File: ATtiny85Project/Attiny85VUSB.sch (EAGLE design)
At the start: 26 parts

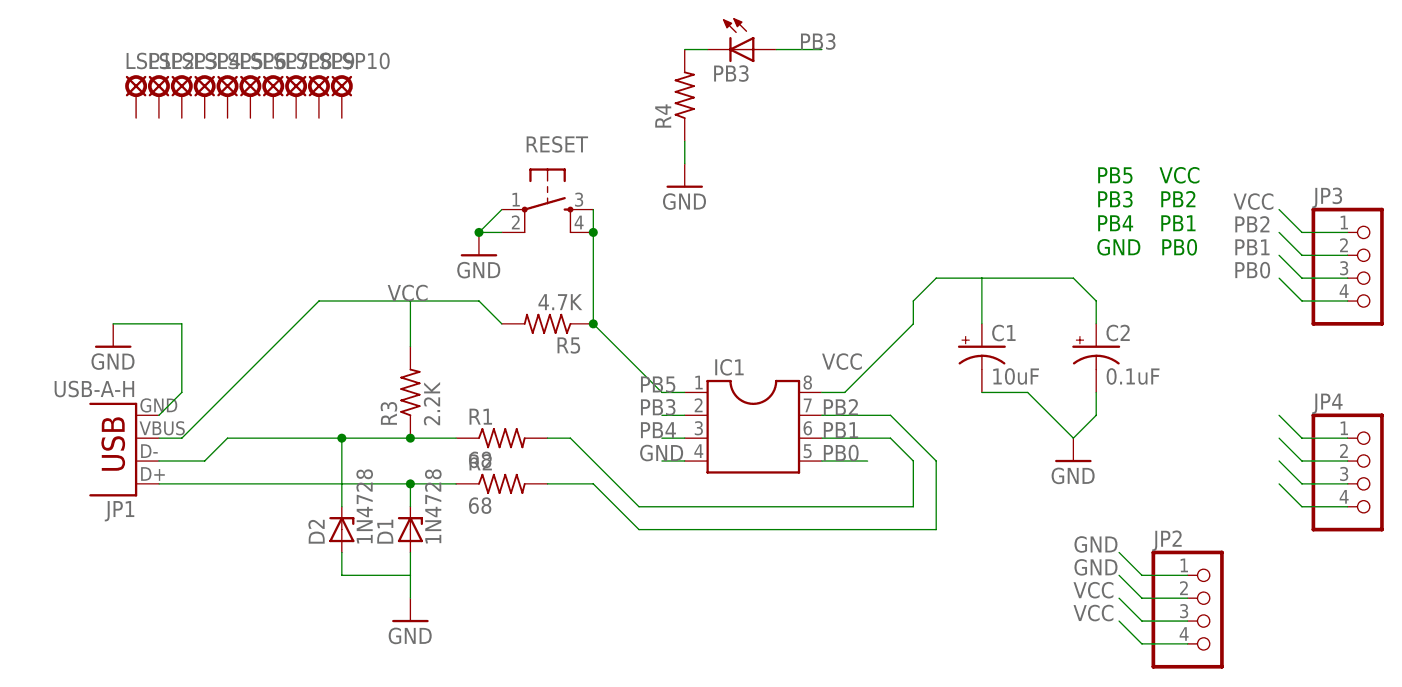
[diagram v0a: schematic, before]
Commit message: Small fixes to attiny85 to use other pins
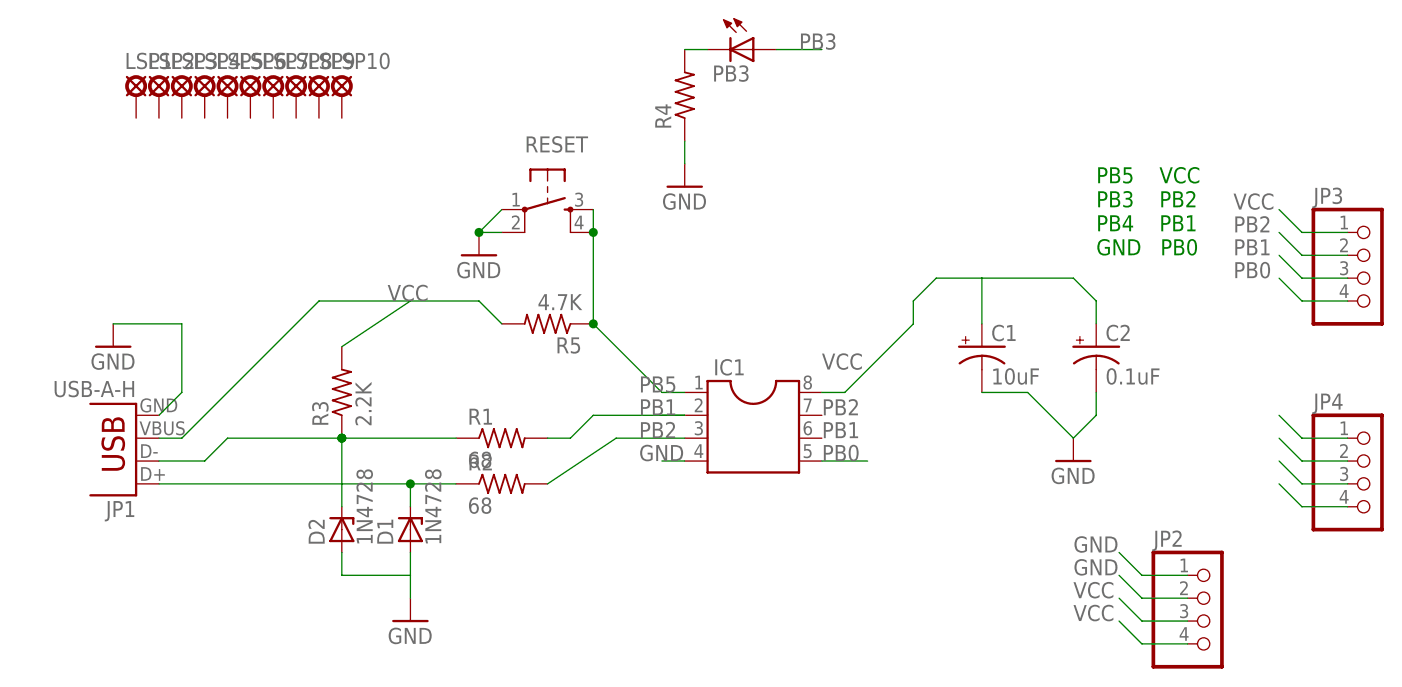
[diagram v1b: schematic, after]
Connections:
- net N$1 renamed DMIN
- net N$4 renamed DPLUS
- net PB1: now also IC1.PB3_CLKI; no longer IC1.PB1_MISO
- net PB2: now also IC1.PB4_CLKO; no longer IC1.PB2SCK
- net PB3: no longer IC1.PB3_CLKI
- net PB4: no longer IC1.PB4_CLKO
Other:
- moved on the sheet: R3
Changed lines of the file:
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@@
 <?xml version="1.0" encoding="utf-8"?>
 <!DOCTYPE eagle SYSTEM "eagle.dtd">
-<eagle version="6.5.0">
+<eagle version="7.5.0">
 <drawing>
 <settings>
@@
 <instance part="R1" gate="G$1" x="7.62" y="68.58"/>
 <instance part="R2" gate="G$1" x="7.62" y="63.5"/>
-<instance part="R3" gate="G$1" x="-2.54" y="73.66" rot="R90"/>
+<instance part="R3" gate="G$1" x="-10.16" y="73.66" rot="R90"/>
 <instance part="D1" gate="1" x="-2.54" y="58.42" rot="R90"/>
 <instance part="D2" gate="1" x="-10.16" y="58.42" rot="R90"/>
@@
 <net name="PB1" class="0">
 <segment>
-<pinref part="IC1" gate="G$1" pin="PB1_MISO"/>
-<wire x1="43.18" y1="68.58" x2="50.8" y2="68.58" width="0.1524" layer="91"/>
-<wire x1="50.8" y1="68.58" x2="53.34" y2="66.04" width="0.1524" layer="91"/>
-<wire x1="53.34" y1="66.04" x2="53.34" y2="60.96" width="0.1524" layer="91"/>
-<wire x1="53.34" y1="60.96" x2="22.86" y2="60.96" width="0.1524" layer="91"/>
-<wire x1="22.86" y1="60.96" x2="15.24" y2="68.58" width="0.1524" layer="91"/>
 <pinref part="R1" gate="G$1" pin="2"/>
-<wire x1="15.24" y1="68.58" x2="12.7" y2="68.58" width="0.1524" layer="91"/>
 <label x="43.18" y="68.58" size="1.778" layer="95"/>
+<wire x1="12.7" y1="68.58" x2="15.24" y2="68.58" width="0.1524" layer="91"/>
+<wire x1="15.24" y1="68.58" x2="17.78" y2="71.12" width="0.1524" layer="91"/>
+<pinref part="IC1" gate="G$1" pin="PB3_CLKI"/>
+<wire x1="27.94" y1="71.12" x2="25.4" y2="71.12" width="0.1524" layer="91"/>
+<label x="22.86" y="71.12" size="1.778" layer="95"/>
+<wire x1="17.78" y1="71.12" x2="27.94" y2="71.12" width="0.1524" layer="91"/>
 </segment>
 <segment>
@@
 <net name="PB2" class="0">
 <segment>
-<pinref part="IC1" gate="G$1" pin="PB2SCK"/>
-<wire x1="43.18" y1="71.12" x2="50.8" y2="71.12" width="0.1524" layer="91"/>
-<wire x1="50.8" y1="71.12" x2="55.88" y2="66.04" width="0.1524" layer="91"/>
-<wire x1="55.88" y1="66.04" x2="55.88" y2="58.42" width="0.1524" layer="91"/>
-<wire x1="55.88" y1="58.42" x2="22.86" y2="58.42" width="0.1524" layer="91"/>
-<wire x1="22.86" y1="58.42" x2="17.78" y2="63.5" width="0.1524" layer="91"/>
 <pinref part="R2" gate="G$1" pin="2"/>
-<wire x1="17.78" y1="63.5" x2="12.7" y2="63.5" width="0.1524" layer="91"/>
 <label x="43.18" y="71.12" size="1.778" layer="95"/>
+<pinref part="IC1" gate="G$1" pin="PB4_CLKO"/>
+<wire x1="27.94" y1="68.58" x2="20.32" y2="68.58" width="0.1524" layer="91"/>
+<label x="22.86" y="68.58" size="1.778" layer="95"/>
+<wire x1="12.7" y1="63.5" x2="20.32" y2="68.58" width="0.1524" layer="91"/>
 </segment>
 <segment>
@@
 </segment>
 </net>
-<net name="N$4" class="0">
+<net name="DPLUS" class="0">
 <segment>
 <pinref part="R2" gate="G$1" pin="1"/>
@@
 </segment>
 </net>
-<net name="N$1" class="0">
+<net name="DMIN" class="0">
 <segment>
 <pinref part="R1" gate="G$1" pin="1"/>
 <pinref part="R3" gate="G$1" pin="1"/>
-<wire x1="2.54" y1="68.58" x2="-2.54" y2="68.58" width="0.1524" layer="91"/>
+<wire x1="2.54" y1="68.58" x2="-10.16" y2="68.58" width="0.1524" layer="91"/>
 <pinref part="D2" gate="1" pin="C"/>
-<wire x1="-2.54" y1="68.58" x2="-10.16" y2="68.58" width="0.1524" layer="91"/>
 <wire x1="-10.16" y1="68.58" x2="-10.16" y2="60.96" width="0.1524" layer="91"/>
 <wire x1="-10.16" y1="68.58" x2="-22.86" y2="68.58" width="0.1524" layer="91"/>
@@
 <wire x1="-25.4" y1="66.04" x2="-30.48" y2="66.04" width="0.1524" layer="91"/>
 <junction x="-10.16" y="68.58"/>
-<junction x="-2.54" y="68.58"/>
+<junction x="-10.16" y="68.58"/>
 </segment>
 </net>
@@
 <segment>
 <pinref part="R3" gate="G$1" pin="2"/>
-<wire x1="-2.54" y1="78.74" x2="-2.54" y2="83.82" width="0.1524" layer="91"/>
+<wire x1="-10.16" y1="78.74" x2="-2.54" y2="83.82" width="0.1524" layer="91"/>
 <label x="-5.08" y="83.82" size="1.778" layer="95"/>
 <pinref part="JP1" gate="G$1" pin="VBUS"/>
@@
 <net name="PB3" class="0">
 <segment>
-<pinref part="IC1" gate="G$1" pin="PB3_CLKI"/>
-<wire x1="27.94" y1="71.12" x2="25.4" y2="71.12" width="0.1524" layer="91"/>
-<label x="22.86" y="71.12" size="1.778" layer="95"/>
-</segment>
-<segment>
 <pinref part="PB3" gate="G$1" pin="A"/>
 <wire x1="38.1" y1="111.76" x2="43.18" y2="111.76" width="0.1524" layer="91"/>
@@
 <net name="PB4" class="0">
 <segment>
-<pinref part="IC1" gate="G$1" pin="PB4_CLKO"/>
-<wire x1="27.94" y1="68.58" x2="25.4" y2="68.58" width="0.1524" layer="91"/>
-<label x="22.86" y="68.58" size="1.778" layer="95"/>
-</segment>
-<segment>
 <pinref part="JP4" gate="A" pin="3"/>

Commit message: Rewire ATtiny85 board to make it compatible with triket
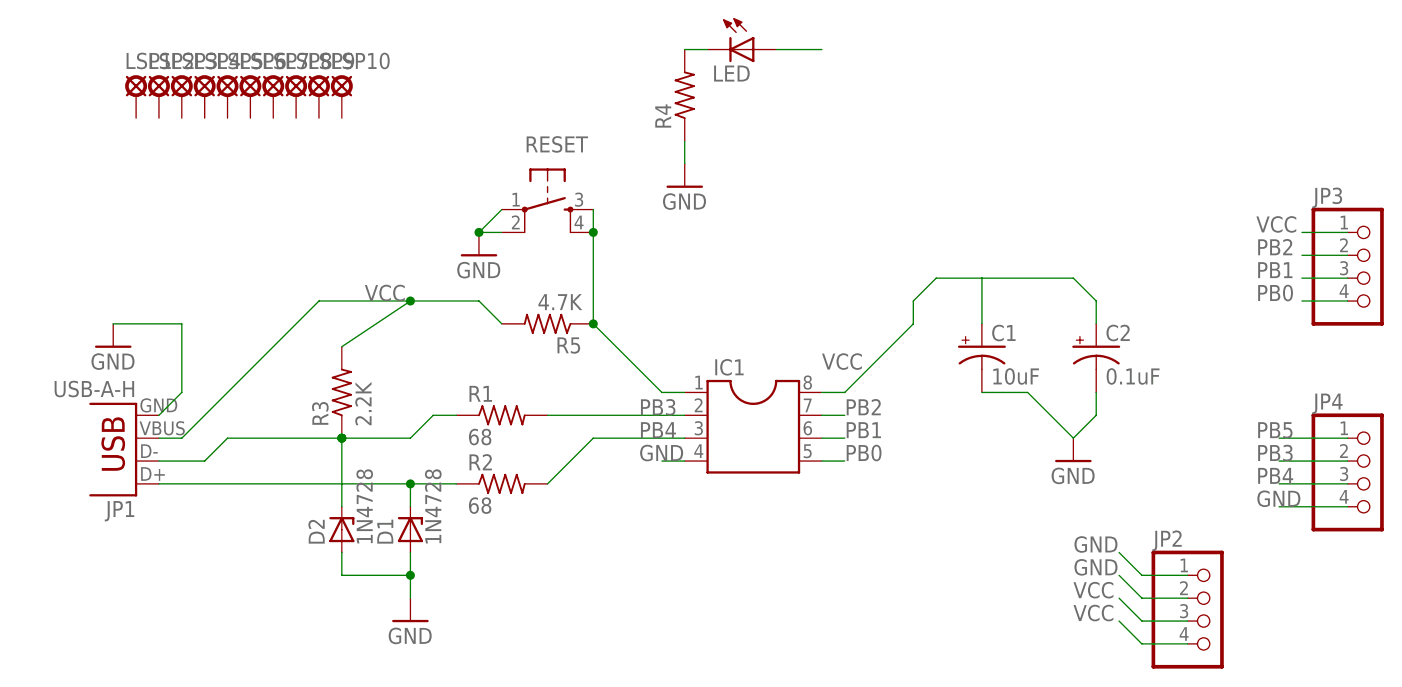
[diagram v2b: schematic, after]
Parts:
- renumbered PB3 to LED
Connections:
- new net RESET: IC1.PB5_~RESET, R5.1, RESET.3, RESET.4
- net PB1: now also IC1.PB1_MISO, LED.A; no longer IC1.PB3_CLKI, R1.2
- net PB2: now also IC1.PB2SCK; no longer IC1.PB4_CLKO, R2.2
- net PB3: now also IC1.PB3_CLKI, R1.2; no longer LED.A
- net PB4: now also IC1.PB4_CLKO, R2.2
- net PB5: no longer IC1.PB5_~RESET, R5.1, RESET.3, RESET.4
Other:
- note removed: "PB5 VCC PB3 PB2 PB4 PB1 GND PB0"
- moved on the sheet: R1
